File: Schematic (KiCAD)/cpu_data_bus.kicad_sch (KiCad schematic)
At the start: 142 parts, among them P13 INVERT, P19 INVERT, P26 INVERT, P5 INVERT, P7 INVERT, X18 INVERT, X19 INVERT, X20 INVERT, X21 INVERT, X22 INVERT, X23 INVERT, X24 INVERT, X25 INVERT, Y11 INVERT, Y12 INVERT, Y18 INVERT, Y19 INVERT, Y25 INVERT, Y26 INVERT, Y4 INVERT, Y5 INVERT

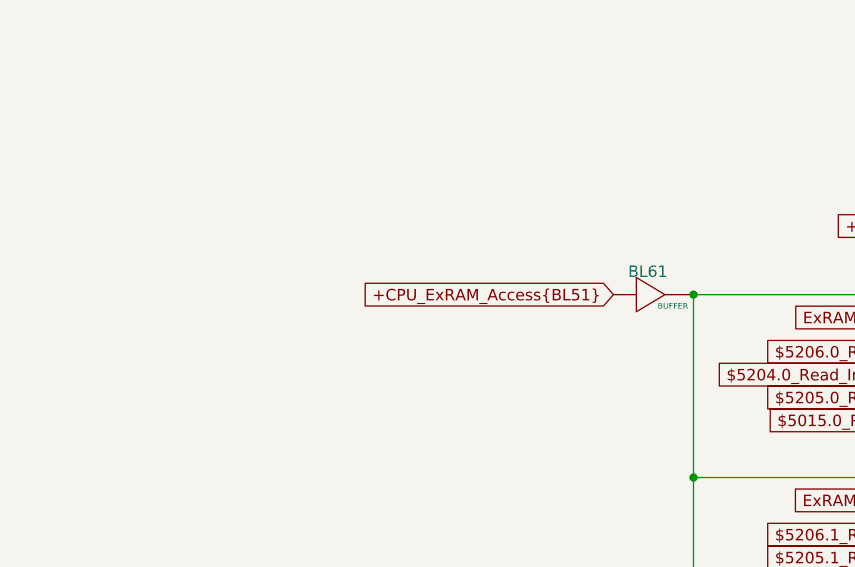
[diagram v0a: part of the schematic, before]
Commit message: - I have fixed all of the problems I was having in the $2006 section, and things are all going places that make sense now.  - I am making good progress on the timer as well.  - I pulled a couple changes back into the letterless SVG and updated the schematic.
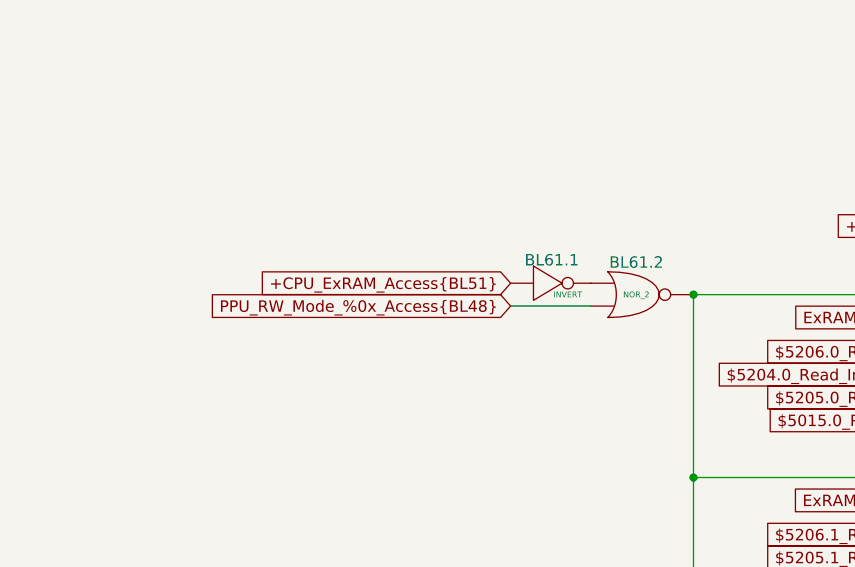
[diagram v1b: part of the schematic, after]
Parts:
- removed BL61: BUFFER, symbol MMC5:BUFFER
- added BL61.1: INVERT, symbol MMC5:INVERT
- added BL61.2: NOR_2, symbol MMC5:NOR_2
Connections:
- net +CPU_ExRAM_Access{BL51}: now also BL61.1. (X)
- net PPU_RW_Mode_%0x_Access{BL48}: now also BL61.2. (X)
- net at BK47. (X): now also BK46. (X); no longer BL50. (X)
- net at BK51. (X): now also BK49. (X); no longer BK52. (X)
- new net: BK55. (X), BK56. (X), BK61. (X), BK62. (X), BK67. (X), BK68. (X), BK73. (X), BK74. (X), BL58. (X)
- new net: BK55. (X), BK56. (X), BK61. (X), BK62. (X), BK67. (X), BK68. (X), BK73. (X), BK74. (X), BL59. (X)
- new net: BK66. (X), BK67. (X)
- new net: BK53. (X), BK58. (X), BK59. (X), BK64. (X), BK65. (X), BK70. (X), BK71. (X), BK76. (X), BL61.2. (X)
- new net: BK63. (X), BK64. (X)
- new net: BK69. (X), BK70. (X)
- new net: BK68. (X), BK69. (X)
- new net: BK65. (X), BK66. (X)
- new net: BL61.1. (X), BL61.2. (X)
- new net: BK57. (X), BK58. (X)
- new net: G15. (X), G16. (X)
- new net: BK75. (X), BK76. (X)
- new net: G10. (X), G9. (X)
- new net: AE15. (X), AE19. (X), G13. (X), MUL20. (X), X19. (X)
- new net: BK47. (X), BL50. (X)
- new net: G1. (X), G2. (X)
- new net: G7. (X), G8. (X)
- new net: G11. (X), G12. (X)
- new net: G5. (X), G6. (X)
- new net: BK53. (X), BK54. (X)
- new net: G3. (X), G4. (X)
- new net: BK48. (X), BP2. (X)
- new net: BP2. (X), BP3. (X)
- new net: BK55. (X), BK73. (X), BK74. (X), BL60. (X)
- new net: BK54. (X), BK55. (X)
- new net: BK72. (X), BK73. (X)
- new net: BK71. (X), BK72. (X)
- new net: BK74. (X), BK75. (X)
- new net: BK74. (X), BL57. (X)
- new net: BK60. (X), BK61. (X)
- new net: BK59. (X), BK60. (X)
- new net: BK56. (X), BK57. (X)
- new net: BK62. (X), BK63. (X)
- new net: BK51. (X), BK52. (X)
- new net: BP1. (X), BP2. (X)
- new net: BK50. (X), BK51. (X)
- new net: BK46. (X), BK51. (X)
- new net: BP2. (X), BP4. (X)
- new net: BK45. (X), BK46. (X)
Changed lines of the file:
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@@
 	)
 	(junction
-		(at 307.34 53.34)
-		(diameter 0)
-		(color 0 0 0 0)
-	)
-	(junction
 		(at 369.57 111.76)
 		(diameter 0)
@@
 	)
 	(junction
+		(at 307.34 53.34)
+		(diameter 0)
+		(color 0 0 0 0)
+	)
+	(junction
 		(at 367.03 114.3)
 		(diameter 0)
@@
 	(wire
 		(pts
+			(xy 287.02 54.61) (xy 295.91 54.61)
+		)
+		(stroke
+			(width 0)
+			(type default)
+		)
+	)
+	(wire
+		(pts
 			(xy 307.34 53.34) (xy 307.34 73.66)
 		)
@@
 		)
 	)
+	(global_label "+CPU_ExRAM_Access{BL51}"
+		(shape input)
+		(at 287.02 52.07 180)
+		(fields_autoplaced yes)
+		(effects
+			(font
+				(size 1.27 1.27)
+			)
+			(justify right)
+		)
+		(property "Intersheetrefs" "${INTERSHEET_REFS}"
+			(at 257.8485 52.07 0)
+			(effects
+				(font
+					(size 1.27 1.27)
+				)
+				(justify right)
+				(hide yes)
+			)
+		)
+	)
 	(global_label "{slash}CPU_D5{AE23}"
 		(shape output)
@@
 		)
 	)
-	(global_label "+CPU_ExRAM_Access{BL51}"
+	(global_label "PPU_RW_Mode_%0x_Access{BL48}"
 		(shape input)
-		(at 298.45 53.34 180)
+		(at 287.02 54.61 180)
 		(fields_autoplaced yes)
 		(effects
@@
 		)
 		(property "Intersheetrefs" "${INTERSHEET_REFS}"
-			(at 269.2785 53.34 0)
+			(at 252.2244 54.61 0)
 			(effects
 				(font
@@
 	)
 	(symbol
+		(lib_id "MMC5:NOR_2")
+		(at 300.99 53.34 0)
+		(unit 1)
+		(exclude_from_sim no)
+		(in_bom yes)
+		(on_board yes)
+		(dnp no)
+		(fields_autoplaced yes)
+		(property "Reference" "BL61.2"
+			(at 300.99 49.022 0)
+			(do_not_autoplace yes)
+			(effects
+				(font
+					(size 1.27 1.27)
+				)
+				(justify top)
+			)
+		)
+		(property "Value" "NOR_2"
+			(at 300.99 53.34 0)
+			(do_not_autoplace yes)
+			(effects
+				(font
+					(size 0.635 0.635)
+				)
+			)
+		)
+		(property "Footprint" ""
+			(at 300.99 53.34 0)
+			(effects
+				(font
+					(size 1.27 1.27)
+				)
+				(hide yes)
+			)
+		)
+		(property "Datasheet" ""
+			(at 300.99 53.34 0)
+			(effects
+				(font
+					(size 1.27 1.27)
+				)
+				(hide yes)
+			)
+		)
+		(property "Description" ""
+			(at 300.99 53.34 0)
+			(effects
+				(font
+					(size 1.27 1.27)
+				)
+				(hide yes)
+			)
+		)
+		(pin ""
+		)
+		(pin ""
+		)
+		(pin ""
+		)
+		(instances
+			(project ""
+				(path "/46093bf6-f83e-4237-9ece-7350a682aff0/f8de81e6-db49-4c78-bf33-f3fdf7c2f2f8"
+					(reference "BL61.2")
+					(unit 1)
+				)
+			)
+		)
+	)
+	(symbol
 		(lib_name "INVERT_80")
 		(lib_id "MMC5:INVERT")
@@
 	)
 	(symbol
+		(lib_name "INVERT_35")
+		(lib_id "MMC5:INVERT")
+		(at 292.1 52.07 0)
+		(unit 1)
+		(exclude_from_sim no)
+		(in_bom yes)
+		(on_board yes)
+		(dnp no)
+		(fields_autoplaced yes)
+		(property "Reference" "BL61.1"
+			(at 291.592 48.768 0)
+			(do_not_autoplace yes)
+			(effects
+				(font
+					(size 1.27 1.27)
+				)
+				(justify top)
+			)
+		)
+		(property "Value" "INVERT"
+			(at 293.37 53.34 0)
+			(do_not_autoplace yes)
+			(effects
+				(font
+					(size 0.635 0.635)
+				)
+			)
+		)
+		(property "Footprint" ""
+			(at 292.1 52.07 0)
+			(effects
+				(font
+					(size 1.27 1.27)
+				)
+				(hide yes)
+			)
+		)
+		(property "Datasheet" ""
+			(at 292.1 52.07 0)
+			(effects
+				(font
+					(size 1.27 1.27)
+				)
+				(hide yes)
+			)
+		)
+		(property "Description" ""
+			(at 292.1 52.07 0)
+			(effects
+				(font
+					(size 1.27 1.27)
+				)
+				(hide yes)
+			)
+		)
+		(pin ""
+		)
+		(pin ""
+		)
+		(instances
+			(project ""
+				(path "/46093bf6-f83e-4237-9ece-7350a682aff0/f8de81e6-db49-4c78-bf33-f3fdf7c2f2f8"
+					(reference "BL61.1")
+					(unit 1)
+				)
+			)
+		)
+	)
+	(symbol
 		(lib_name "BUFFER_2")
 		(lib_id "MMC5:BUFFER")
@@
 					(unit 1)
 				)
-			)
-		)
-	)
-	(symbol
-		(lib_name "BUFFER_17")
-		(lib_id "MMC5:BUFFER")
-		(at 302.26 53.34 0)
-		(unit 1)
-		(exclude_from_sim no)
-		(in_bom yes)
-		(on_board yes)
-		(dnp no)
-		(fields_autoplaced yes)
-		(property "Reference" "BL61"
-			(at 302.26 50.038 0)
-			(do_not_autoplace yes)
-			(effects
-				(font
-					(size 1.27 1.27)
-				)
-				(justify top)
-			)
-		)
-		(property "Value" "BUFFER"
-			(at 305.054 54.61 0)
-			(do_not_autoplace yes)
-			(effects
-				(font
-					(size 0.635 0.635)
-				)
-			)
-		)
-		(property "Footprint" ""
-			(at 302.26 53.34 0)
-			(effects
-				(font
-					(size 1.27 1.27)
-				)
-				(hide yes)
-			)
-		)
-		(property "Datasheet" ""
-			(at 302.26 53.34 0)
-			(effects
-				(font
-					(size 1.27 1.27)
-				)
-				(hide yes)
-			)
-		)
-		(property "Description" ""
-			(at 302.26 53.34 0)
-			(effects
-				(font
-					(size 1.27 1.27)
-				)
-				(hide yes)
-			)
-		)
-		(pin ""
-		)
-		(pin ""
-		)
-		(instances
-			(project ""
-				(path "/46093bf6-f83e-4237-9ece-7350a682aff0/f8de81e6-db49-4c78-bf33-f3fdf7c2f2f8"
-					(reference "BL61")
-					(unit 1)
-				)

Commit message: I fixed 2 errors in the letterless MMC5 tracing:
1. BK5 is a NAND-4 gate.  It was thought to be NAND-3 before.
2.  BL83 and BL96 signals got swapped here before.  They actually cross each other:

BL83 = "PPU_RW_Mode_%0x_Access"
BL96 = "+ExRAM_Mode_$0x"

This propagated out to several changes in the schematic.
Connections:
- net +ExRAM_Mode_$0x{BL48}: now reaches BL61.2. (X)
- net +ExRAM_Mode_$0x{BL48}: now also BK50. (X), BL48. (X); no longer BL61.1. (X)
- net at BK47. (X): now also BK46. (X); no longer BL50. (X)
- net at BK51. (X): now also BK49. (X); no longer BK52. (X)
- removed net PPU_RW_Mode_%0x_Access{BL48}: BK50. (X), BL48. (X), BL61.2. (X)
- net PPU_RW_Mode_%0x_Access{BL83} renamed +ExRAM_Mode_$0x{BL96}
- new net: BK55. (X), BK56. (X), BK61. (X), BK62. (X), BK67. (X), BK68. (X), BK73. (X), BK74. (X), BL58. (X)
- new net: BK55. (X), BK56. (X), BK61. (X), BK62. (X), BK67. (X), BK68. (X), BK73. (X), BK74. (X), BL59. (X)
- new net: BK66. (X), BK67. (X)
- new net: BK53. (X), BK58. (X), BK59. (X), BK64. (X), BK65. (X), BK70. (X), BK71. (X), BK76. (X), BL61.2. (X)
- new net: BK63. (X), BK64. (X)
- new net: BK69. (X), BK70. (X)
- new net: BK68. (X), BK69. (X)
- new net: BK65. (X), BK66. (X)
- new net: BL61.1. (X), BL61.2. (X)
- new net: BK57. (X), BK58. (X)
- new net: G15. (X), G16. (X)
- new net: BK75. (X), BK76. (X)
- new net: G10. (X), G9. (X)
- new net: AE15. (X), AE19. (X), G13. (X), MUL20. (X), X19. (X)
- new net: BK47. (X), BL50. (X)
- new net: G1. (X), G2. (X)
- new net: G7. (X), G8. (X)
- new net: G11. (X), G12. (X)
- new net: G5. (X), G6. (X)
- new net: BK53. (X), BK54. (X)
- new net: G3. (X), G4. (X)
- new net: BK48. (X), BP2. (X)
- new net: BP2. (X), BP3. (X)
- new net: BK55. (X), BK73. (X), BK74. (X), BL60. (X)
- new net: BK54. (X), BK55. (X)
- new net: BK72. (X), BK73. (X)
- new net: BK71. (X), BK72. (X)
- new net: BK74. (X), BK75. (X)
- new net: BK74. (X), BL57. (X)
- new net: BK60. (X), BK61. (X)
- new net: BK59. (X), BK60. (X)
- new net: BK56. (X), BK57. (X)
- new net: BK62. (X), BK63. (X)
- new net: BK51. (X), BK52. (X)
- new net: BP1. (X), BP2. (X)
- new net: BK50. (X), BK51. (X)
- new net: BK46. (X), BK51. (X)
- new net: BP2. (X), BP4. (X)
- new net: BK45. (X), BK46. (X)
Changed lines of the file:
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@@
 		)
 	)
-	(global_label "PPU_RW_Mode_%0x_Access{BL48}"
+	(global_label "+ExRAM_Mode_$0x{BL48}"
 		(shape output)
 		(at 208.28 204.47 0)
@@
 		)
 		(property "Intersheetrefs" "${INTERSHEET_REFS}"
-			(at 243.0756 204.47 0)
+			(at 235.4555 204.47 0)
 			(effects
 				(font
@@
 		)
 	)
-	(global_label "PPU_RW_Mode_%0x_Access{BL48}"
+	(global_label "+ExRAM_Mode_$0x{BL48}"
 		(shape input)
 		(at 287.02 54.61 180)
@@
 		)
 		(property "Intersheetrefs" "${INTERSHEET_REFS}"
-			(at 252.2244 54.61 0)
+			(at 259.8445 54.61 0)
 			(effects
 				(font
@@
 		)
 	)
-	(global_label "PPU_RW_Mode_%0x_Access{BL83}"
+	(global_label "+ExRAM_Mode_$0x{BL96}"
 		(shape input)
 		(at 198.12 207.01 180)
@@
 		)
 		(property "Intersheetrefs" "${INTERSHEET_REFS}"
-			(at 163.3244 207.01 0)
-			(effects
-				(font
+			(at 170.9445 207.01 0)
+			(effects
+				(font

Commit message: Tracing and schematic updates.  - Added timer to schematic.  - Added all items from artifacts sheet to the MMC5A trace.
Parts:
- removed B30, E65: INVERT, symbol MMC5:INVERT
- added TF1, TF2, TF3, TF4, TF5, TF6, TF7, TF8: BUFFER, symbol MMC5:BUFFER
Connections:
- net +CPU_D4{B30} is gone; now on net /CPU_D4{X22}: X22. (X)
- net CPU_D0_IN_PIN: now also TF1. (X)
- net CPU_D2_IN_PIN: now also TF3. (X)
- net CPU_D3_IN_PIN: now also TF4. (X)
- net CPU_D4_IN_PIN: now also X22. (X), TF5. (X)
- net CPU_D5_IN_PIN: now also TF6. (X)
- net CPU_D6_IN_PIN: now also TF7. (X)
- net CPU_D7_IN_PIN: now also TF8. (X)
- net at BK47. (X): now also BK46. (X); no longer BL50. (X)
- net at BK51. (X): now also BK49. (X); no longer BK52. (X)
- net +PCM_IRQ_If_Enabled{K114} renamed +PCM_IRQ_Status_Bit{K114}
- new net: BK55. (X), BK56. (X), BK61. (X), BK62. (X), BK67. (X), BK68. (X), BK73. (X), BK74. (X), BL58. (X)
- new net: BK55. (X), BK56. (X), BK61. (X), BK62. (X), BK67. (X), BK68. (X), BK73. (X), BK74. (X), BL59. (X)
- new net: BK66. (X), BK67. (X)
- new net: BK53. (X), BK58. (X), BK59. (X), BK64. (X), BK65. (X), BK70. (X), BK71. (X), BK76. (X), BL61.2. (X)
- new net: BK63. (X), BK64. (X)
- new net: BK69. (X), BK70. (X)
- new net: BK68. (X), BK69. (X)
- new net: BK65. (X), BK66. (X)
- new net: BL61.1. (X), BL61.2. (X)
- new net: BK57. (X), BK58. (X)
- new net: G15. (X), G16. (X)
- new net: BK75. (X), BK76. (X)
- new net: G10. (X), G9. (X)
- new net: AE15. (X), AE19. (X), G13. (X), MUL20. (X), TF2. (X), X19. (X)
- new net: BK47. (X), BL50. (X)
- new net: G1. (X), G2. (X)
- new net: G7. (X), G8. (X)
- new net: G11. (X), G12. (X)
- new net: G5. (X), G6. (X)
- new net: BK53. (X), BK54. (X)
- new net: G3. (X), G4. (X)
- new net: BK48. (X), BP2. (X)
- new net: BP2. (X), BP3. (X)
- new net: BK55. (X), BK73. (X), BK74. (X), BL60. (X)
- new net: BK54. (X), BK55. (X)
- new net: BK72. (X), BK73. (X)
- new net: BK71. (X), BK72. (X)
- new net: BK74. (X), BK75. (X)
- new net: BK74. (X), BL57. (X)
- new net: BK60. (X), BK61. (X)
- new net: BK59. (X), BK60. (X)
- new net: BK56. (X), BK57. (X)
- new net: BK62. (X), BK63. (X)
- new net: BK51. (X), BK52. (X)
- new net: BP1. (X), BP2. (X)
- new net: BK50. (X), BK51. (X)
- new net: BK46. (X), BK51. (X)
- new net: BP2. (X), BP4. (X)
- new net: BK45. (X), BK46. (X)
- new net +CPU_D0{TF1}: TF1. (X)
- new net +CPU_D1{TF2}: TF2. (X)
- new net +CPU_D2{TF3}: TF3. (X)
- new net +CPU_D3{TF4}: TF4. (X)
- new net +CPU_D4{TF5}: TF5. (X)
- new net +CPU_D5{TF6}: TF6. (X)
- new net +CPU_D6{TF7}: TF7. (X)
- new net +CPU_D7{TF8}: TF8. (X)
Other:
- note added: "MMC5A Only"
- moved on the sheet: AE15, AE19, AE20, AE21, AE22, AE23, AE24, AE25, D3, E1, E17, E2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
